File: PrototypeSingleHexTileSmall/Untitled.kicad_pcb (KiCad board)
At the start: 2 copper layers, 40.6 x 35.2 mm, 12 parts

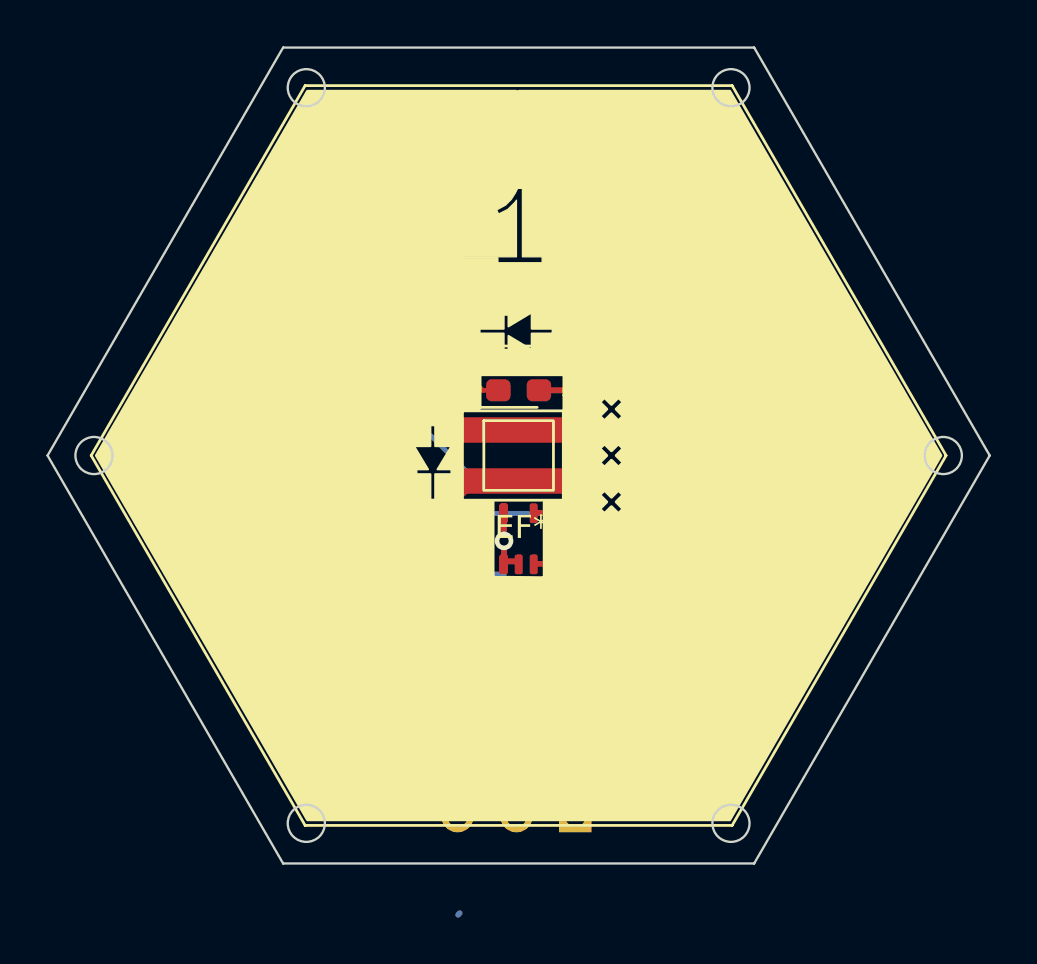
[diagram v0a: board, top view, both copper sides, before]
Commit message: v5 of the prototype hexboard and squareboards:  added label to capacitors and resistors; moved temperature sensors to periphery; added 0.1 mm back to top and bottom of boards
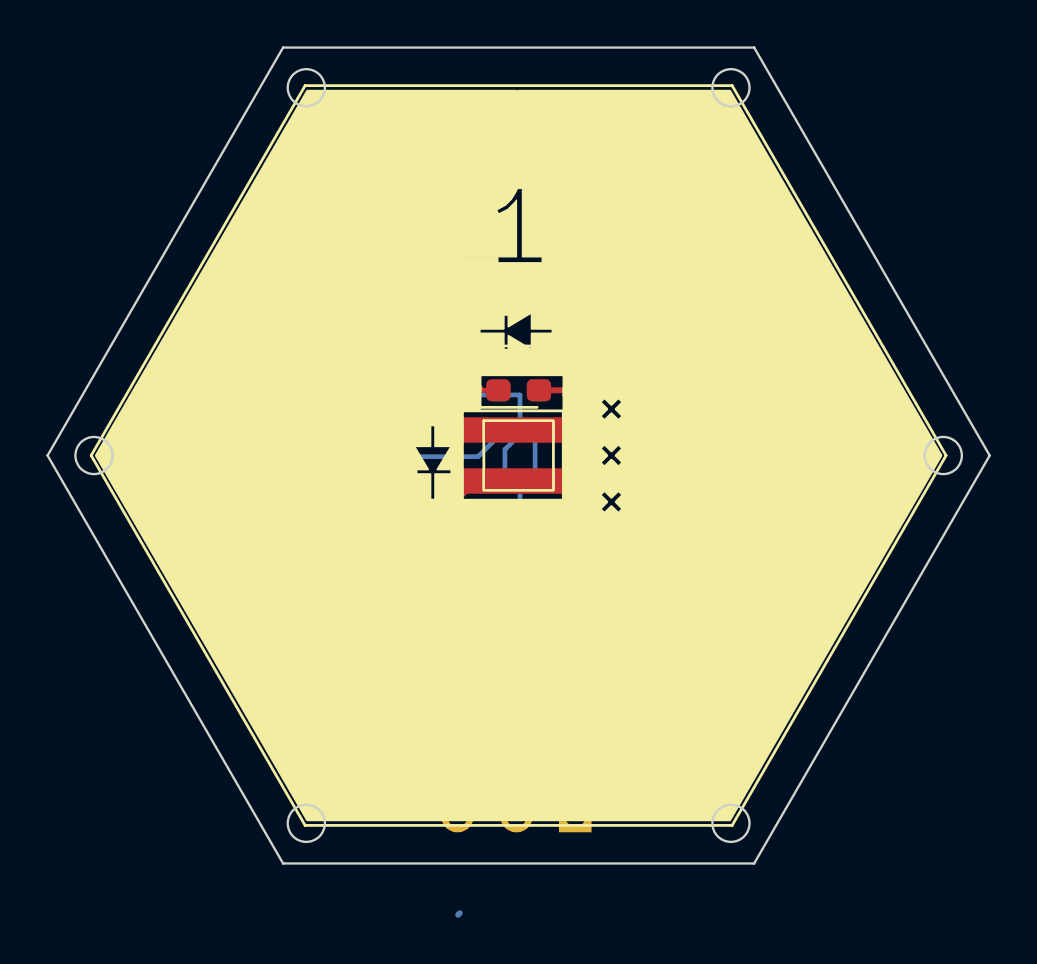
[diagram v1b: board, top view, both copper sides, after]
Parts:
- removed ? (x2): , 
- REF**: moved to B.Cu
- REF**: value R_0402_1005Metric -> R_1206_3216Metric; footprint Resistor_SMD:R_0402_1005Metric -> Resistor_SMD:R_1206_3216Metric
- moved REF** 3.60 mm to (103.8, 58.0), turned to 180 degrees
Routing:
- net (no net): track 215.1 -> 209.1 mm, vias 4 -> 1
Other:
- board text added: "Designed by Sebouh J. Paul v2 sidelength=20.30 mm"
- board text removed: "Designed by Sebouh J. Paul sidelength =20.30 mm"
